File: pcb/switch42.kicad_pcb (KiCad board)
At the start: 2 copper layers, 114.3 x 76.2 mm, 84 parts, among them J1 MJ-4PP-9, SW1 SW_PUSH, SW10 SW_PUSH, SW11 SW_PUSH, SW12 SW_PUSH, SW13 SW_PUSH, SW14 SW_PUSH, SW15 SW_PUSH, SW16 SW_PUSH, SW17 SW_PUSH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

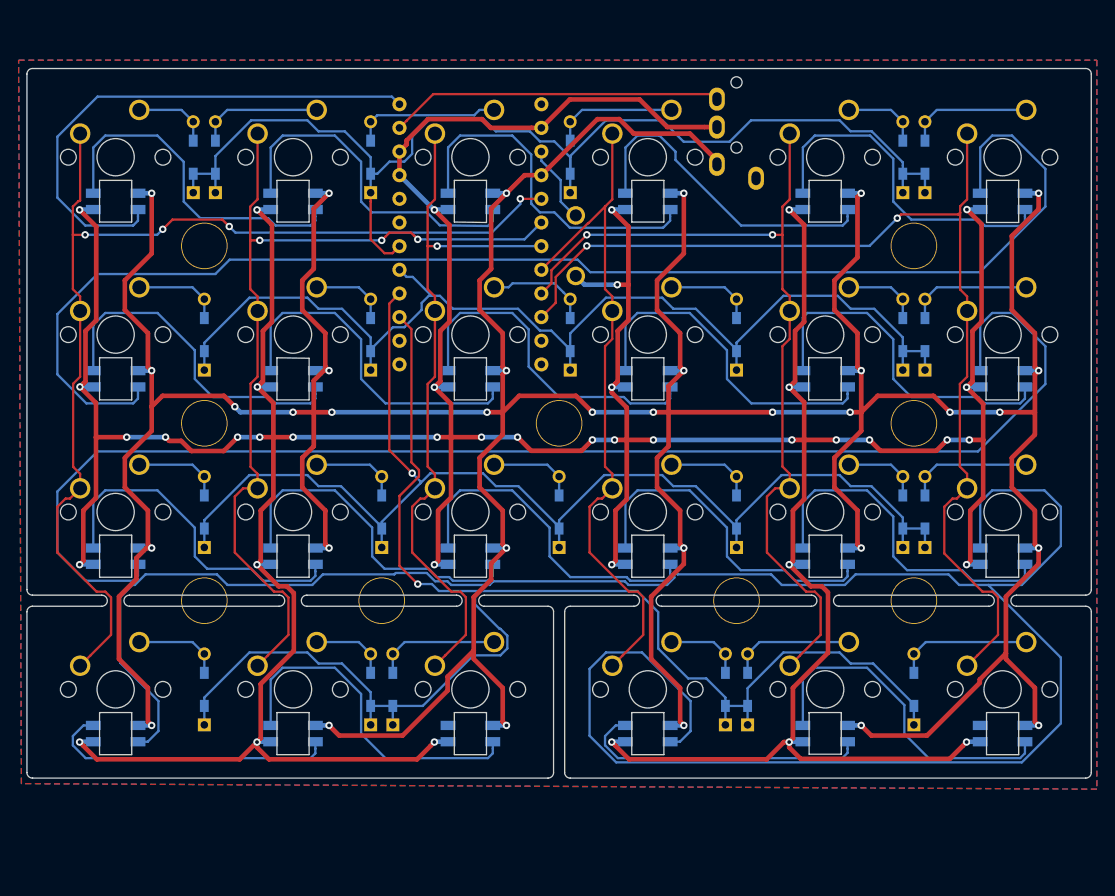
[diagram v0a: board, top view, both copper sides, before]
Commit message: Add margin and mask, silk to the pcb
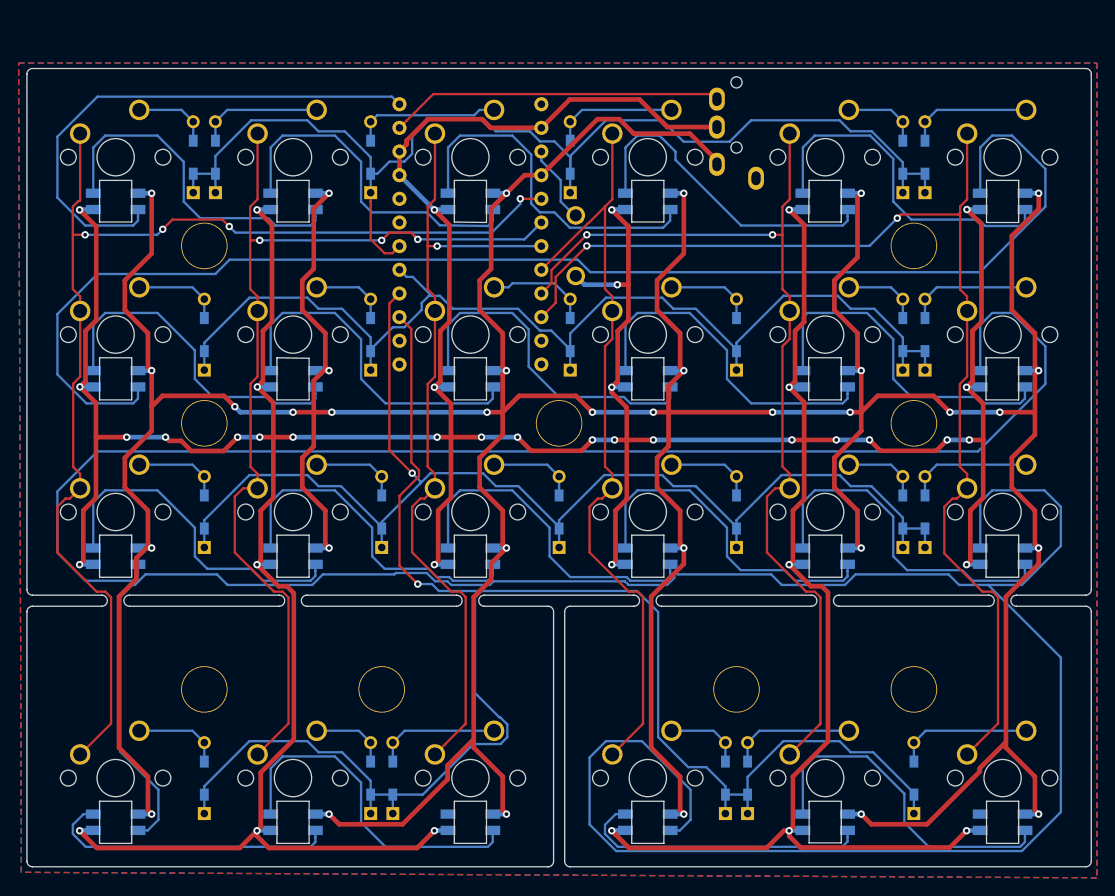
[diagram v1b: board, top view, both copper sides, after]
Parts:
- moved D12 9.53 mm to (90.5, 111.3)
- moved D16 9.53 mm to (126.2, 111.3)
- moved D20 9.53 mm to (128.6, 111.3)
- moved D24 9.53 mm to (146.5, 111.3)
- moved D4 9.53 mm to (70.3, 111.3)
- moved D8 9.53 mm to (88.1, 111.3)
- moved L12 9.53 mm to (98.9, 116.0)
- moved L16 9.53 mm to (117.9, 116.0)
- moved L20 9.53 mm to (137.0, 116.0)
- moved L24 9.53 mm to (156.0, 116.0)
- moved L4 9.53 mm to (60.8, 116.0)
- moved L8 9.53 mm to (79.8, 116.0)
- moved Ref** 9.53 mm to (146.5, 101.7)
- moved Ref** 9.53 mm to (127.4, 101.7)
- moved Ref** 9.53 mm to (89.3, 101.7)
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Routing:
- net VCC: track 548.6 -> 586.7 mm
- net GND: track 561.0 -> 580.0 mm
- net row3: track 160.7 -> 179.8 mm
- net Net-(L16-Pad3): track 244.2 -> 263.2 mm
- net col4: track 94.0 -> 103.7 mm
- net col3: track 73.7 -> 83.4 mm
- net col2: track 76.3 -> 86.0 mm
- net col1: track 97.9 -> 107.4 mm
- net col0: track 117.5 -> 127.0 mm
- net col5: track 115.3 -> 124.9 mm
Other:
- board size 114.3 x 76.2 mm -> 114.3 x 85.7 mm
- board text added: "L"
- board text added: "R"
- board text added: "switch42 designed by @zk_phi"

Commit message: Change skrew positions and thumb margin
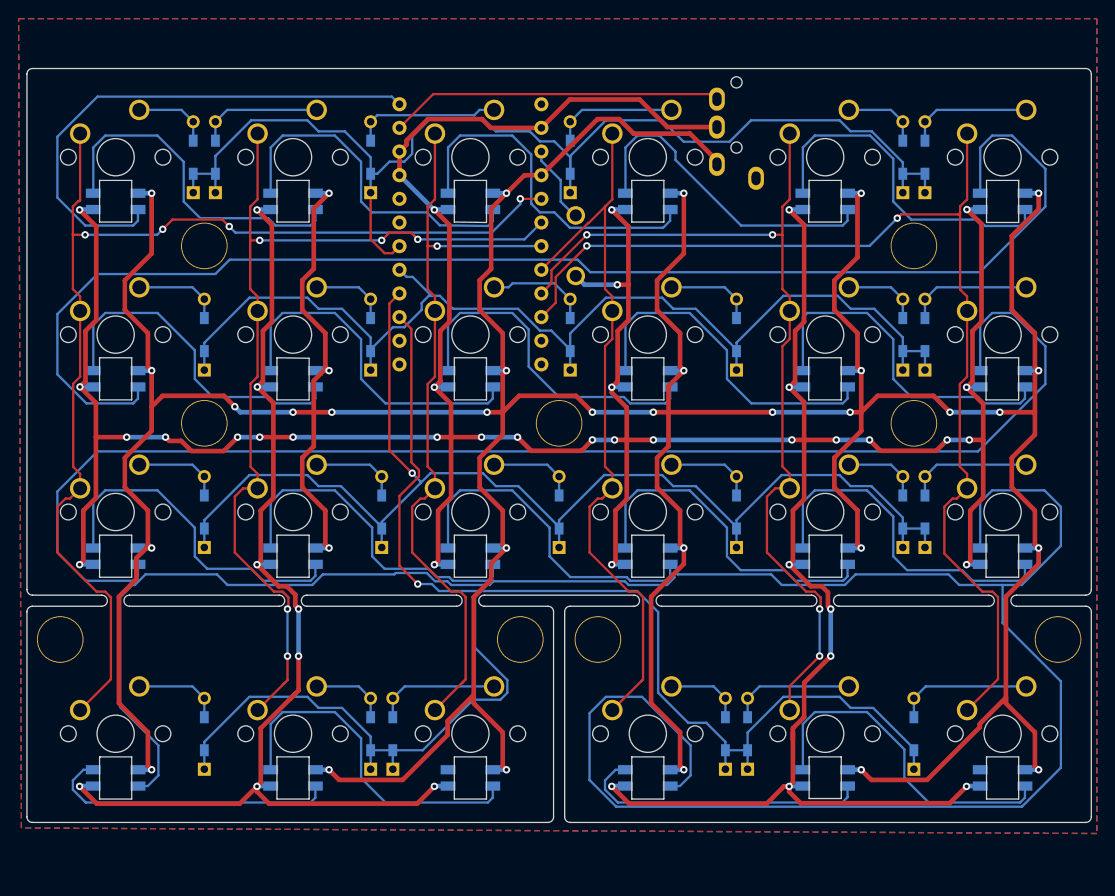
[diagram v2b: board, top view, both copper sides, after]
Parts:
- moved Ref** 16.4 mm to (162.0, 96.4)
- moved Ref** 16.4 mm to (54.8, 96.4)
- moved Ref** 15.8 mm to (112.5, 96.4)
- moved Ref** 15.8 mm to (104.2, 96.4)
- moved D12 4.76 mm to (90.5, 106.5)
- moved D16 4.76 mm to (126.2, 106.5)
- moved D20 4.76 mm to (128.6, 106.5)
- moved D24 4.76 mm to (146.5, 106.5)
- moved D4 4.76 mm to (70.3, 106.5)
- moved D8 4.76 mm to (88.1, 106.5)
- moved L12 4.76 mm to (98.9, 111.2)
- moved L16 4.76 mm to (117.9, 111.2)
- moved L20 4.76 mm to (137.0, 111.2)
- moved L24 4.76 mm to (156.0, 111.2)
- moved L4 4.76 mm to (60.8, 111.2)
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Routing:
- net VCC: track 586.7 -> 568.3 mm
- net Net-(L16-Pad3): track 263.2 -> 253.0 mm
- net row3: track 179.8 -> 170.2 mm
- net GND: track 580.0 -> 572.9 mm, vias 41 -> 45
- net col4: track 103.7 -> 98.8 mm, vias 2 -> 4
- net col3: track 83.4 -> 78.6 mm
- net col5: track 124.9 -> 120.1 mm
- net col0: track 127.0 -> 122.3 mm
- net col1: track 107.4 -> 102.8 mm, vias 3 -> 5
- net col2: track 86.0 -> 81.5 mm
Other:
- board size 114.3 x 85.7 mm -> 114.3 x 81 mm
- board text added: "* switch42 designed by @zk_phi *"
- board text removed: "switch42 designed by @zk_phi"

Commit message: Change footprint of TRRS and ProMicro
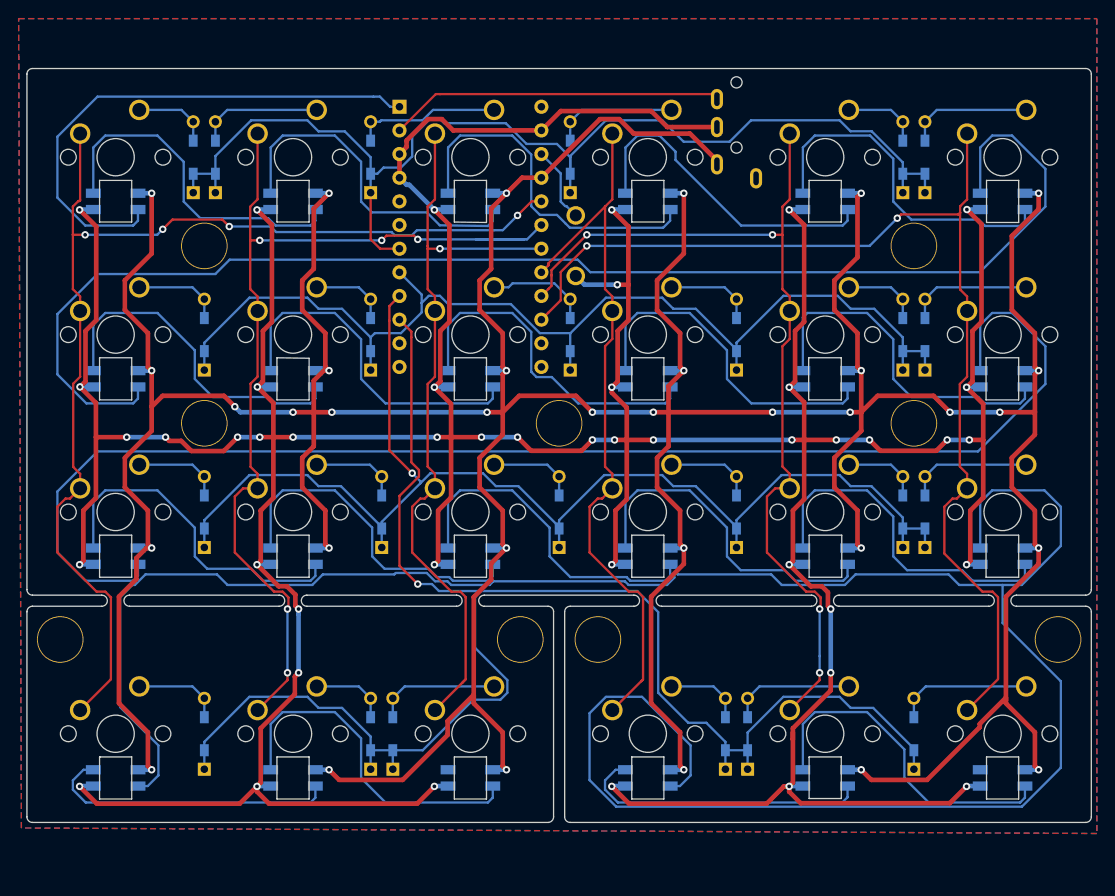
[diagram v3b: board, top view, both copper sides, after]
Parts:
- J1: footprint kbd:MJ-4PP-9-irreversible -> SMKJP:CON_MJ-4PP-9-kbd; moved to B.Cu
- U1: footprint kbd:ProMicro_v2_irreversible -> SMKJP:BOARD_Pro_Micro_Reversed-conthrough; moved to B.Cu
- moved U1 16.8 mm to (98.9, 35.3), turned to 270 degrees
- moved J1 1.75 mm to (127.4, 35.0), turned to 270 degrees
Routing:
- net col1: track 102.8 -> 106.9 mm
- net GND: track 572.9 -> 571.3 mm
- net row1: track 118.2 -> 116.8 mm
- net row3: track 170.2 -> 169.6 mm

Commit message: Add silks to the switches, and adjust promicro/trrs position
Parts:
- moved J1 2.10 mm to (127.4, 37.1)
- moved U1 1.20 mm to (99.0, 36.5)
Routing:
- net col3: track 78.9 -> 82.4 mm
- net GND: track 571.3 -> 574.2 mm
- net data: track 36.2 -> 38.9 mm
- net VCC: track 568.3 -> 570.0 mm
- net row3: track 169.6 -> 168.3 mm
- net reset: track 8.33 -> 7.09 mm
- net col0: track 122.0 -> 123.2 mm
- net col5: track 120.4 -> 121.5 mm
- net col4: track 99.1 -> 100.2 mm
- net Net-(L2-Pad3): track 147.9 -> 148.7 mm
- net row1: track 116.8 -> 115.9 mm
- net Net-(L10-Pad1): track 37.3 -> 36.4 mm
- net col2: track 81.5 -> 82.4 mm
- net Net-(L13-Pad3): track 38.2 -> 37.5 mm
- net row0: track 121.8 -> 122.5 mm
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
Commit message: Thinner silks for promicro and thinner margin between two thumb clusters
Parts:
- moved Ref** 0.30 mm to (112.3, 96.4)
- moved Ref** 0.30 mm to (104.5, 96.4)
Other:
- outline, holes or cut-outs redrawn
- board text added: "* switch42 v0.2 designed by @zk_phi *"
- board text removed: "* switch42 designed by @zk_phi *"
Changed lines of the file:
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@@
     (fp_line (start -1.27 3.81) (end -1.27 -3.81) (layer Cmts.User) (width 0.3))
     (fp_line (start 2.54 3.81) (end -1.27 3.81) (layer Cmts.User) (width 0.3))
-    (fp_line (start 2.54 8.89) (end 2.54 6.35) (layer B.SilkS) (width 0.3))
-    (fp_line (start 5.08 8.89) (end 5.08 6.35) (layer B.SilkS) (width 0.3))
-    (fp_line (start 2.54 6.35) (end 5.08 6.35) (layer B.SilkS) (width 0.3))
-    (fp_line (start 33.02 8.89) (end 0 8.89) (layer B.SilkS) (width 0.3))
-    (fp_line (start 33.02 -8.89) (end 33.02 8.89) (layer B.SilkS) (width 0.3))
-    (fp_line (start 0 -8.89) (end 33.02 -8.89) (layer B.SilkS) (width 0.3))
-    (fp_line (start 0 8.89) (end 0 -8.89) (layer B.SilkS) (width 0.3))
+    (fp_line (start 2.54 8.89) (end 2.54 6.35) (layer B.SilkS) (width 0.1))
+    (fp_line (start 5.08 8.89) (end 5.08 6.35) (layer B.SilkS) (width 0.1))
+    (fp_line (start 2.54 6.35) (end 5.08 6.35) (layer B.SilkS) (width 0.1))
+    (fp_line (start 33.02 8.89) (end 0 8.89) (layer B.SilkS) (width 0.1))
+    (fp_line (start 33.02 -8.89) (end 33.02 8.89) (layer B.SilkS) (width 0.1))
+    (fp_line (start 0 -8.89) (end 33.02 -8.89) (layer B.SilkS) (width 0.1))
+    (fp_line (start 0 8.89) (end 0 -8.89) (layer B.SilkS) (width 0.1))
     (pad 13 thru_hole circle (at 31.75 -7.62 270) (size 1.524 1.524) (drill 0.8128) (layers *.Cu *.Mask)
       (net 45 "Net-(U1-Pad13)"))
@@
       (effects (font (size 1 1) (thickness 0.15)) (justify mirror))
     )
-    (fp_line (start 0 -2.5) (end 0 2.5) (layer B.Fab) (width 0.1))
+    (fp_line (start 0 -2.5) (end 0 2.5) (layer B.SilkS) (width 0.1))
     (fp_line (start -2 -2.5) (end 0 -2.5) (layer B.Fab) (width 0.1))
     (fp_line (start -2 2.5) (end -2 -2.5) (layer B.Fab) (width 0.1))
@@
     (fp_line (start 0 3) (end 12 3) (layer B.SilkS) (width 0.1))
     (fp_line (start 0 -3) (end 12 -3) (layer B.SilkS) (width 0.1))
-    (fp_line (start 0 -3) (end 0 -2.5) (layer B.Fab) (width 0.1))
-    (fp_line (start 0 3) (end 0 2.5) (layer B.Fab) (width 0.1))
+    (fp_line (start 0 -3) (end 0 -2.5) (layer B.SilkS) (width 0.1))
+    (fp_line (start 0 3) (end 0 2.5) (layer B.SilkS) (width 0.1))
     (pad A thru_hole oval (at 11.8 -2.1 270) (size 2.2 1.3) (drill oval 1.5 0.6) (layers *.Cu *.Mask)
       (net 30 "Net-(J1-PadA)"))
@@
   )
   (module kbd:HOLE (layer F.Cu)
-    (at 112.549292 96.369492)
+    (at 112.251634 96.369492)
     (descr "Mounting Hole 2.2mm, no annular, M2")
     (tags "mounting hole 2.2mm no annular m2")
@@
   )
   (module kbd:HOLE (layer F.Cu)
-    (at 104.214868 96.369492)
+    (at 104.512526 96.369492)
     (descr "Mounting Hole 2.2mm, no annular, M2")
     (tags "mounting hole 2.2mm no annular m2")
@@
     (effects (font (size 5 5) (thickness 0.3)) (justify mirror))
   )
-  (gr_text "* switch42 designed by @zk_phi *" (at 136.957248 95.17886) (layer F.Mask)
+  (gr_text "* switch42 v0.2 designed by @zk_phi *" (at 136.957248 95.17886) (layer F.Mask)
     (effects (font (size 1.2 1.2) (thickness 0.3)))
   )
-  (gr_text "* switch42 designed by @zk_phi *" (at 79.806912 95.17886) (layer F.Mask)
+  (gr_text "* switch42 v0.2 designed by @zk_phi *" (at 79.806912 95.17886) (layer F.Mask)
     (effects (font (size 1.2 1.2) (thickness 0.3)))
   )
-  (gr_line (start 108.977396 115.419604) (end 108.977396 93.392912) (layer Edge.Cuts) (width 0.1))
-  (gr_line (start 107.786764 93.392912) (end 107.786764 115.419604) (layer Edge.Cuts) (width 0.1))
+  (gr_line (start 108.679738 115.419604) (end 108.679738 93.392912) (layer Edge.Cuts) (width 0.1))
+  (gr_line (start 108.084422 93.392912) (end 108.084422 115.419604) (layer Edge.Cuts) (width 0.1))
   (dimension 85.725504 (width 0.3) (layer F.SilkS)
     (gr_text "85.726 mm" (at 46.452822 77.914696 270) (layer F.SilkS)
@@
     (arrow2b (pts (xy 51.231744 32.075365) (xy 52.358248 31.488944)))
   )
-  (gr_arc (start 109.572712 93.392912) (end 109.572712 92.797596) (angle -90) (layer Edge.Cuts) (width 0.1))
-  (gr_arc (start 107.191448 93.392912) (end 107.786764 93.392912) (angle -90) (layer Edge.Cuts) (width 0.1))
+  (gr_arc (start 109.275054 93.392912) (end 109.275054 92.797596) (angle -90) (layer Edge.Cuts) (width 0.1))
+  (gr_arc (start 107.489106 93.392912) (end 108.084422 93.392912) (angle -90) (layer Edge.Cuts) (width 0.1))
   (gr_arc (start 164.9371 91.011648) (end 164.9371 91.606964) (angle -90) (layer Edge.Cuts) (width 0.1))
   (gr_arc (start 157.49565 92.20228) (end 157.49565 91.606964) (angle -180) (layer Edge.Cuts) (width 0.1))
@@
   (gr_arc (start 119.395426 92.20228) (end 119.395426 91.606964) (angle -180) (layer Edge.Cuts) (width 0.1))
   (gr_arc (start 164.9371 115.419604) (end 164.9371 116.01492) (angle -90) (layer Edge.Cuts) (width 0.1))
-  (gr_arc (start 109.572712 115.419604) (end 108.977396 115.419604) (angle -90) (layer Edge.Cuts) (width 0.1))
+  (gr_arc (start 109.275054 115.419604) (end 108.679738 115.419604) (angle -90) (layer Edge.Cuts) (width 0.1))
   (gr_arc (start 116.418846 92.20228) (end 116.418846 92.797596) (angle -180) (layer Edge.Cuts) (width 0.1))
   (gr_arc (start 100.345314 92.20228) (end 100.345314 91.606964) (angle -180) (layer Edge.Cuts) (width 0.1))
-  (gr_arc (start 107.191448 115.419604) (end 107.191448 116.01492) (angle -90) (layer Edge.Cuts) (width 0.1))
+  (gr_arc (start 107.489106 115.419604) (end 107.489106 116.01492) (angle -90) (layer Edge.Cuts) (width 0.1))
   (gr_arc (start 97.368734 92.20228) (end 97.368734 92.797596) (angle -180) (layer Edge.Cuts) (width 0.1))
   (gr_arc (start 81.295202 92.20228) (end 81.295202 91.606964) (angle -180) (layer Edge.Cuts) (width 0.1))
@@
   (gr_line (start 119.395426 92.797596) (end 135.468958 92.797596) (layer Edge.Cuts) (width 0.1))
   (gr_line (start 100.345314 91.606964) (end 116.418846 91.606964) (layer Edge.Cuts) (width 0.1))
-  (gr_line (start 100.345314 92.797596) (end 107.191448 92.797596) (layer Edge.Cuts) (width 0.1))
-  (gr_line (start 164.9371 116.01492) (end 109.572712 116.01492) (layer Edge.Cuts) (width 0.1))
-  (gr_line (start 109.572712 92.797596) (end 116.418846 92.797596) (layer Edge.Cuts) (width 0.1))
+  (gr_line (start 100.345314 92.797596) (end 107.489106 92.797596) (layer Edge.Cuts) (width 0.1))
+  (gr_line (start 164.9371 116.01492) (end 109.275054 116.01492) (layer Edge.Cuts) (width 0.1))
+  (gr_line (start 109.275054 92.797596) (end 116.418846 92.797596) (layer Edge.Cuts) (width 0.1))
   (gr_line (start 97.368734 91.606964) (end 81.295202 91.606964) (layer Edge.Cuts) (width 0.1))
   (gr_line (start 81.295202 92.797596) (end 97.368734 92.797596) (layer Edge.Cuts) (width 0.1))
@@
   (gr_line (start 59.26851 92.797596) (end 51.82706 92.797596) (layer Edge.Cuts) (width 0.1))
   (gr_line (start 51.82706 91.606964) (end 59.26851 91.606964) (layer Edge.Cuts) (width 0.1))
-  (gr_line (start 51.82706 116.01492) (end 107.191448 116.01492) (layer Edge.Cuts) (width 0.1))
+  (gr_line (start 51.82706 116.01492) (end 107.489106 116.01492) (layer Edge.Cuts) (width 0.1))
   (gr_line (start 51.231744 35.64726) (end 51.231744 91.011648) (layer Edge.Cuts) (width 0.1))
   (gr_line (start 165.532416 35.64726) (end 165.532416 91.011648) (layer Edge.Cuts) (width 0.1))
